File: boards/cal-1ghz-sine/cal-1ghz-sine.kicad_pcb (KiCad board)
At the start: 4 copper layers, 43 x 12 mm, 17 parts, among them J1 CONN_01X01, J2 SMA, J3 CONN_01X01, U1 MIC5305-3.3YML-TR, U2 CCSO-914X3-1000

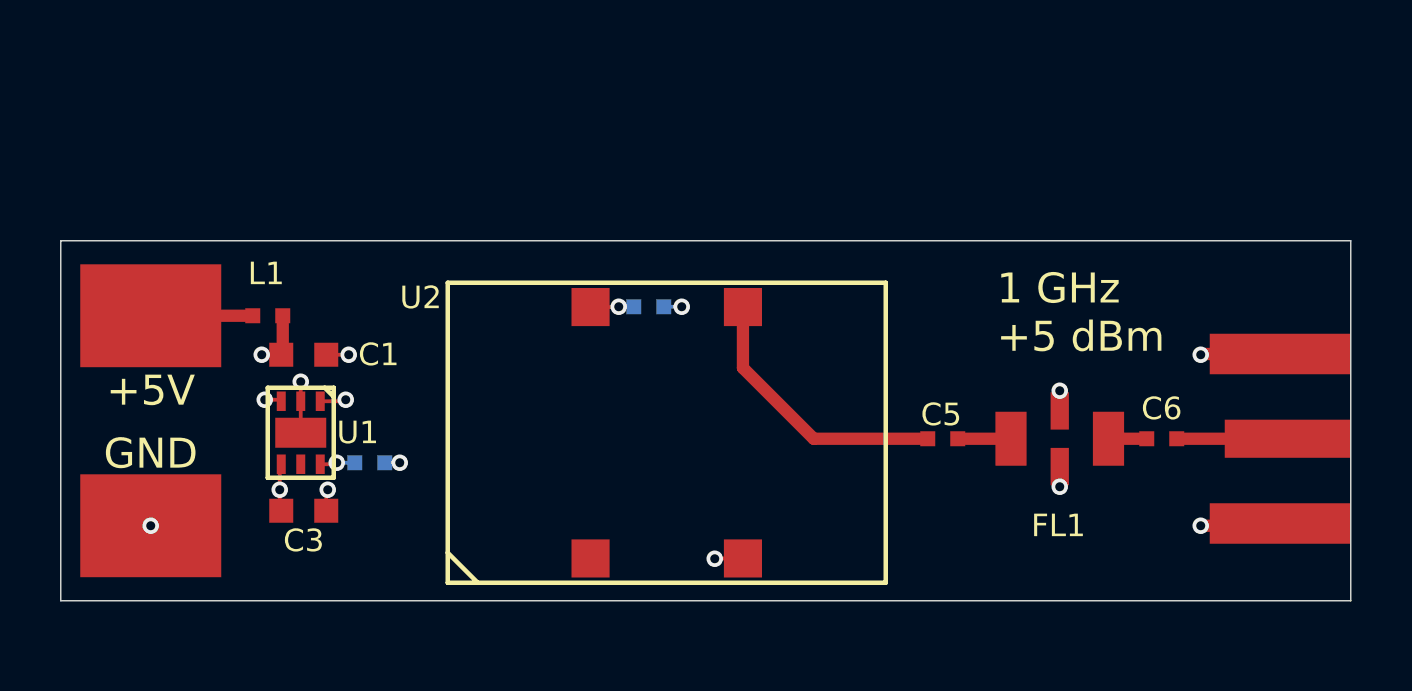
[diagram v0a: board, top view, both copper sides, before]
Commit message: Finished initial version of cal-1ghz-sine board. Sending to fab.
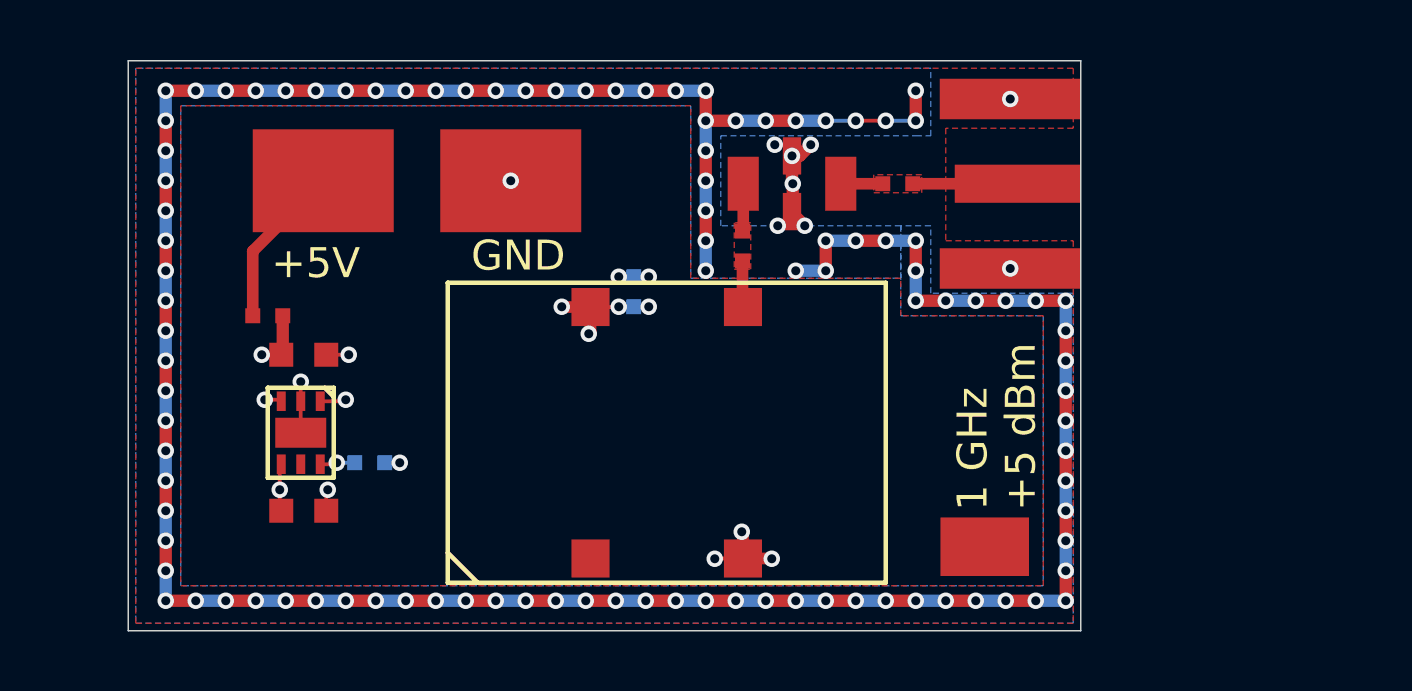
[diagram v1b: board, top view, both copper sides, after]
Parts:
- added REF**: SERIALNUM_MOLEX_0916580020, azonenberg_pcb:SERIALNUM_MOLEX_0916580020, F.Cu at (55.8, 35.7)
- moved G*** 17.5 mm to (43.2, 22.7)
- moved J3 16.6 mm to (40.0, 23.5)
- moved J2 12.4 mm to (59.0, 23.6)
- moved FL1 12.3 mm to (49.4, 23.6)
- moved C6 12.2 mm to (52.9, 23.6)
- moved C5 9.26 mm to (47.7, 25.7), turned to 270 degrees
- moved J1 7.30 mm to (33.8, 23.5)
- moved G*** 6.70 mm to (32.2, 33.5)
- moved G*** 6.16 mm to (33.2, 25.2)
- moved G*** 5.71 mm to (38.2, 34.4)
- moved C4 0.71 mm to (44.1, 27.2), turned to 90 degrees
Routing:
- net /GND: track 78.0 -> 162.5 mm, vias 11 -> 120
- net /CLK_DC: track 9.17 -> 1.54 mm
- net /3V3: track 18.7 -> 25.3 mm, vias 2 -> 5
- net /5V0_RAW: track 3.40 -> 5.47 mm
- added copper zone on B.Cu, net /GND
- added copper zone on F.Cu, net /GND
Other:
- board size 43 x 12 mm -> 31.8 x 19 mm
- board text added: "FREESAMPLE Timebase Calibration Std A. Zonenberg 2018-12-06 / v0.1"
- board text removed: "FREESAMPLE Timebase Calibration Standard A. Zonenberg 2018-12-05 / v0.1"
